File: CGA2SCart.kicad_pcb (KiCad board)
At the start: 2 copper layers, 57.1 x 62.2 mm, 25 parts, among them J1 SCART-F, J2 DB9_Male, J3 Audio-Jack-3_2Switches, Q1 2N7000

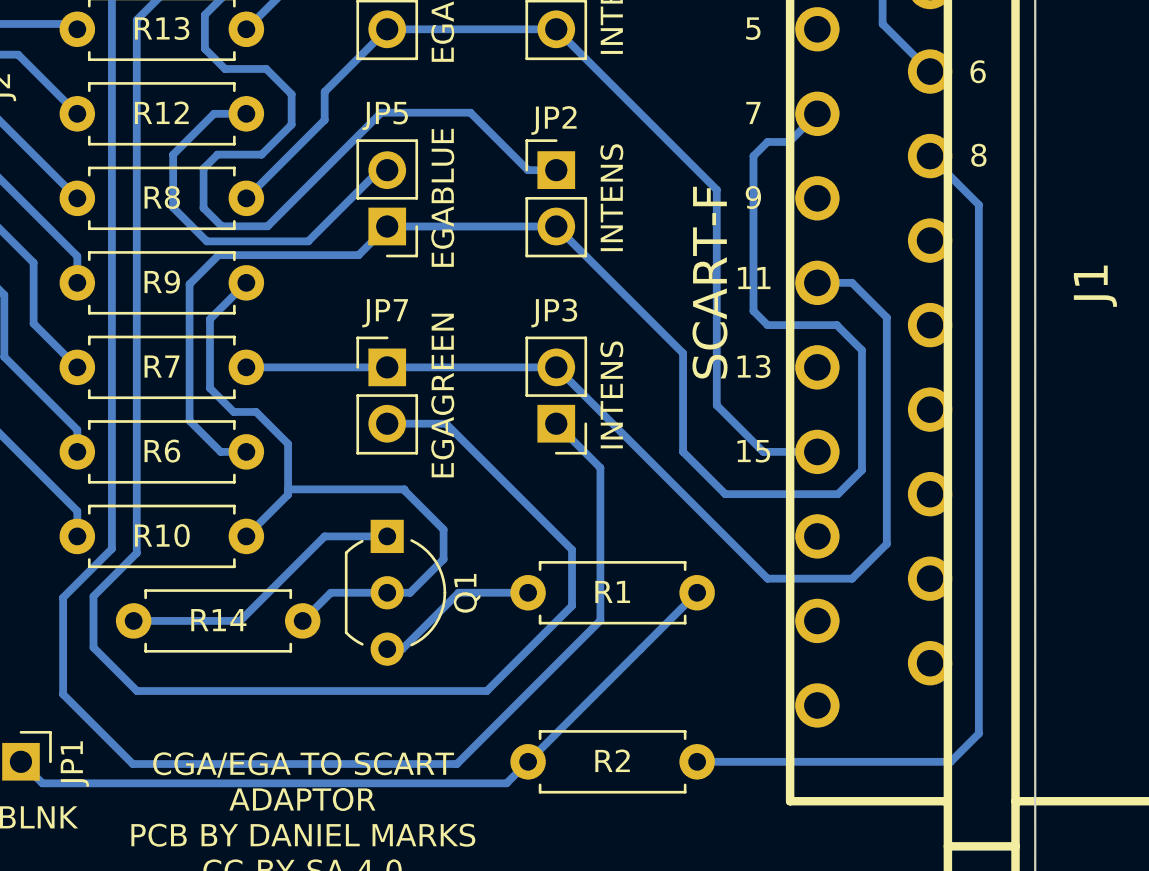
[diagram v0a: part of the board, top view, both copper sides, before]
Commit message: Corrected sync problem
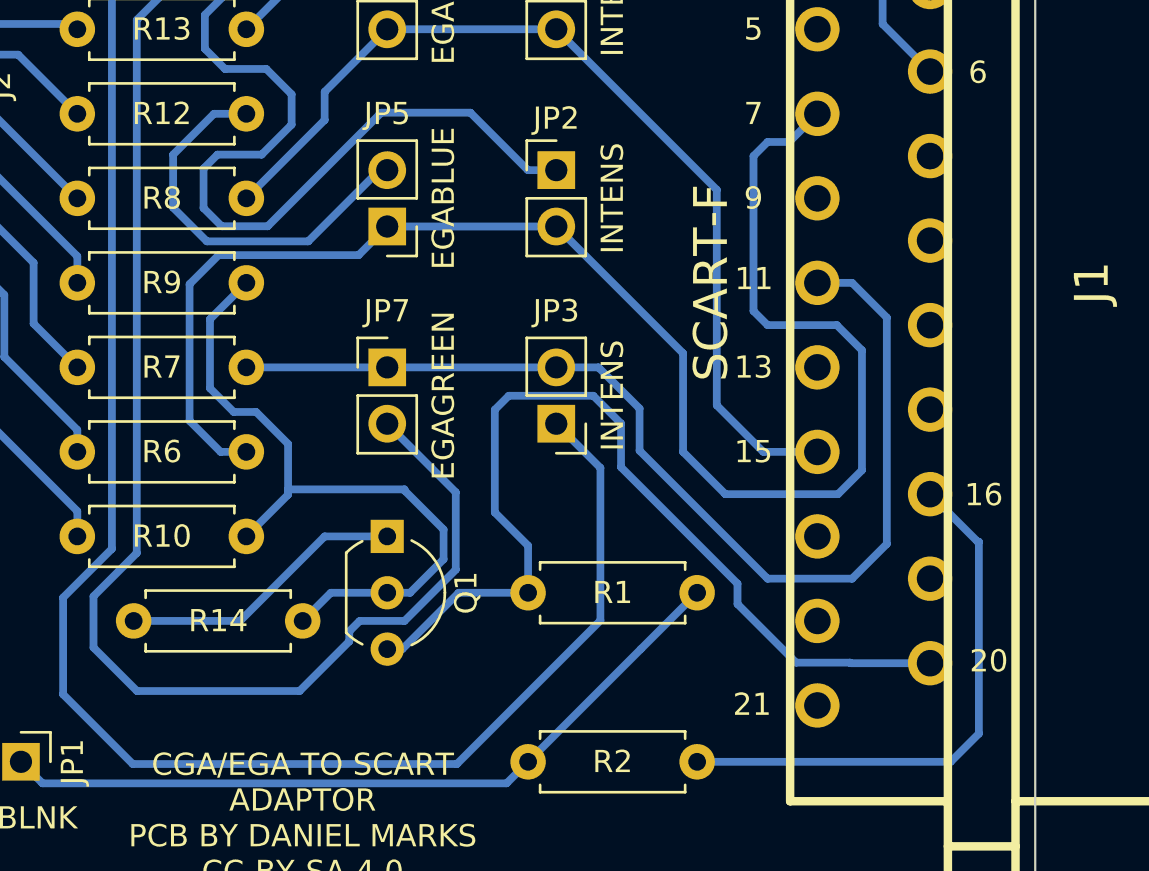
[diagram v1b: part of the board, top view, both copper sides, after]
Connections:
- J1 pad 16: unconnected-(J1-Pad16) -> Net-(J1-Pad16)
- J1 pad 20: unconnected-(J1-Pad20) -> Net-(Q1-Pad3)
- J1 pad 21: unconnected-(J1-Pad21) -> GND
- J1 pad 8: Net-(J1-Pad8) -> unconnected-(J1-Pad8)
- R2 pad 1: Net-(J1-Pad8) -> Net-(J1-Pad16)
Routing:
- net Net-(J1-Pad8): track 40.2 -> 0.00 mm
- net Net-(Q1-Pad3): track 7.40 -> 42.8 mm
- net Net-(J1-Pad16): track 0.00 -> 25.0 mm
- net Net-(JP7-Pad2): track 72.6 -> 63.0 mm
- net Net-(J1-Pad11): track 47.4 -> 48.6 mm
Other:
- board text added: "16"
- board text added: "20"
- board text added: "21"
- board text removed: "8"

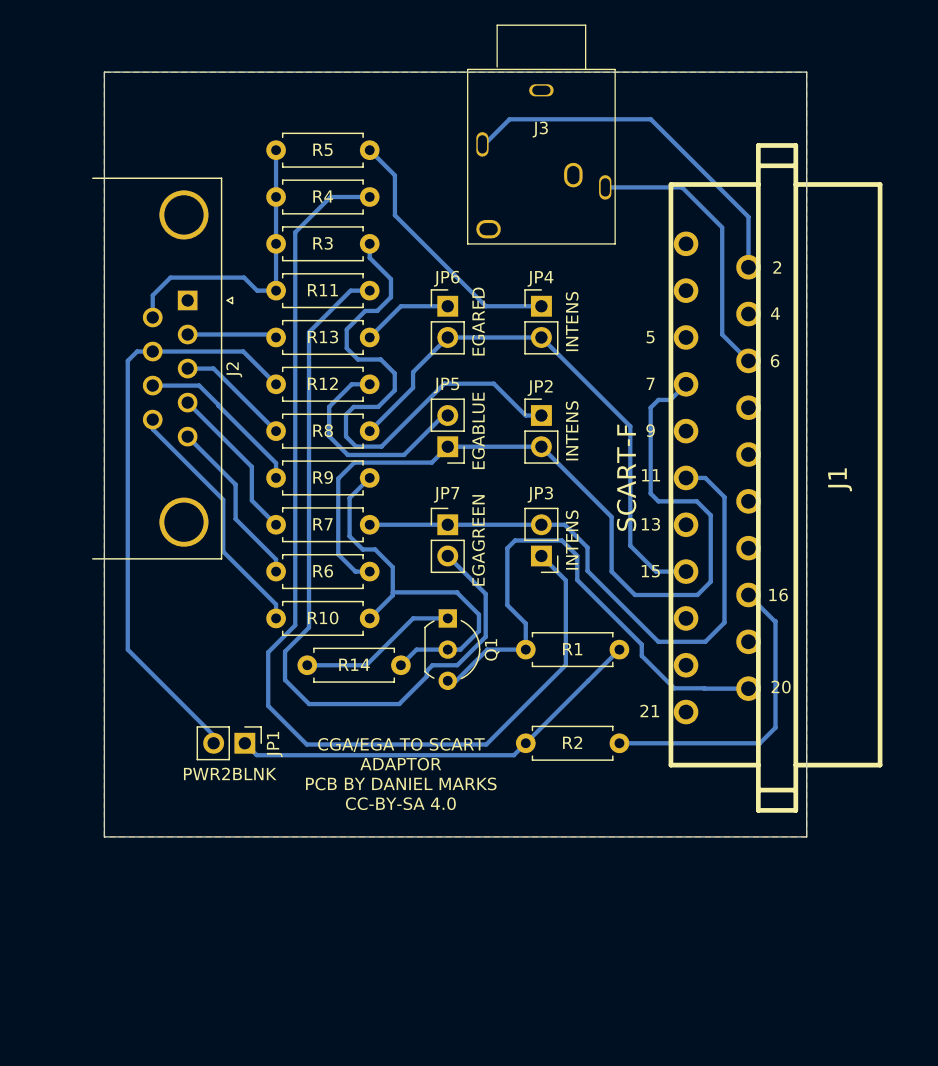
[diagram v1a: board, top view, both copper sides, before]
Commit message: Added a VGA port
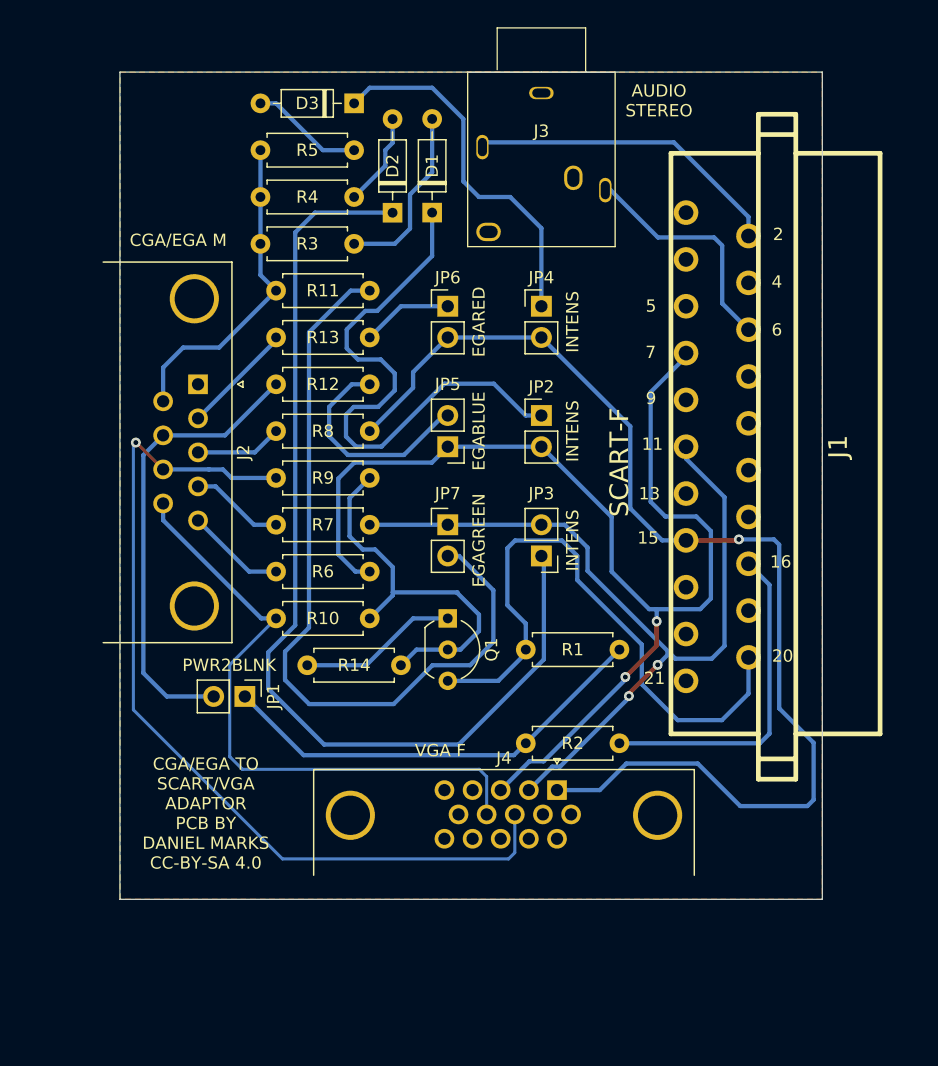
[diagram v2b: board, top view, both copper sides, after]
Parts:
- added D1: 1N4148, Diode_THT:D_DO-35_SOD27_P7.62mm_Horizontal, F.Cu at (127.0, 59.7)
- added D2: 1N4148, Diode_THT:D_DO-35_SOD27_P7.62mm_Horizontal, F.Cu at (123.8, 59.7)
- added D3: 1N4148, Diode_THT:D_DO-35_SOD27_P7.62mm_Horizontal, F.Cu at (120.7, 50.8)
- added J4: DB15_Female_HighDensity, Connector_Dsub:DSUB-15-HD_Female_Horizontal_P2.29x1.98mm_EdgePinOffset3.03mm_Housed_MountingHolesOffset4.94mm, F.Cu at (137.2, 106.7)
- R3, R4, R5: value 1k -> 330R
- moved J2 6.87 mm to (108.0, 73.7)
- moved JP1 3.81 mm to (111.8, 99.1)
- moved J1 2.54 mm to (154.9, 78.7)
- moved R3 1.27 mm to (113.0, 62.2)
- moved R4 1.27 mm to (113.0, 58.4)
- moved R5 1.27 mm to (113.0, 54.6)
- moved J3 0.22 mm to (135.9, 48.3)
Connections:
- R3 pad 2: Net-(JP2-Pad1) -> Net-(R3-Pad2)
- R4 pad 2: Net-(JP3-Pad1) -> Net-(R4-Pad2)
- R5 pad 2: Net-(JP4-Pad1) -> Net-(R5-Pad2)
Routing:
- net Net-(J2-Pad8): track 13.9 -> 73.8 mm, vias 0 -> 1
- net Net-(J1-Pad15): track 43.2 -> 93.5 mm, vias 0 -> 1
- net Net-(J2-Pad9): track 20.3 -> 51.3 mm
- net Net-(J1-Pad7): track 70.4 -> 94.5 mm, vias 0 -> 2
- net Net-(J1-Pad11): track 48.6 -> 68.8 mm, vias 0 -> 2
- net Net-(R3-Pad2): track 0.00 -> 14.7 mm
- net Net-(J2-Pad7): track 47.5 -> 37.4 mm
- net Net-(R5-Pad2): track 0.00 -> 9.20 mm
- net Net-(JP4-Pad1): track 21.1 -> 29.8 mm
- net Net-(R4-Pad2): track 0.00 -> 7.64 mm
- net Net-(J1-Pad20): track 42.8 -> 49.3 mm
- net Net-(R6-Pad1): track 14.0 -> 8.07 mm
- net Net-(J2-Pad4): track 12.9 -> 7.64 mm
- net Net-(J1-Pad2): track 29.9 -> 25.9 mm
- net Net-(J1-Pad6): track 22.6 -> 19.1 mm
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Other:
- board size 57.1 x 62.2 mm -> 57.2 x 67.3 mm
- board text added: "AUDIO STEREO"
- board text added: "CGA/EGA M"
- board text added: "CGA/EGA TO SCART/VGA ADAPTOR PCB BY DANIEL MARKS CC-BY-SA 4.0"
- board text added: "VGA F"
- board text removed: "CGA/EGA TO SCART ADAPTOR PCB BY DANIEL MARKS CC-BY-SA 4.0"

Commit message: Put SCART connector on the right way...
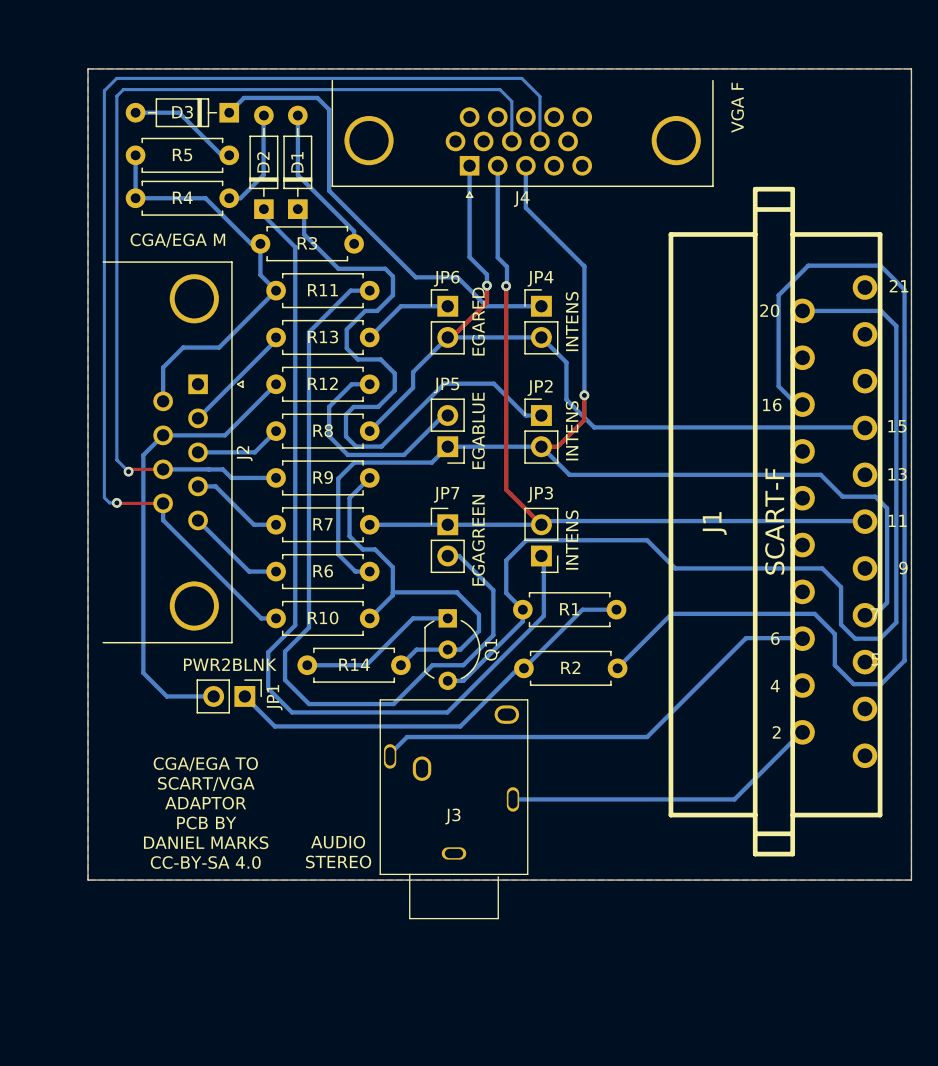
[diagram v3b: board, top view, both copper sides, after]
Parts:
- moved J3 65.7 mm to (128.8, 113.5), turned to 180 degrees
- moved J4 51.3 mm to (130.0, 55.9), turned to 180 degrees
- moved D1 10.9 mm to (116.1, 59.4)
- moved D2 10.5 mm to (113.3, 59.4)
- moved D3 10.2 mm to (110.5, 51.6)
- moved R5 10.2 mm to (102.9, 55.0)
- moved R4 10.2 mm to (102.9, 58.5)
- moved R2 6.10 mm to (142.1, 96.8)
- moved J1 6.10 mm to (154.9, 84.8), turned to -90 degrees
- moved R1 3.26 mm to (142.0, 92.0)
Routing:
- net Net-(J1-Pad16): track 27.1 -> 81.5 mm
- net Net-(J2-Pad9): track 51.3 -> 92.1 mm, vias 0 -> 1
- net Net-(J1-Pad20): track 49.3 -> 84.7 mm
- net Net-(J1-Pad15): track 93.5 -> 64.3 mm
- net Net-(J1-Pad6): track 19.1 -> 36.9 mm
- net Net-(D2-Pad1): track 82.3 -> 72.4 mm
- net Net-(J2-Pad6): track 26.5 -> 34.1 mm
- net Net-(D3-Pad1): track 29.8 -> 36.8 mm
- net Net-(J2-Pad8): track 73.8 -> 79.3 mm
- net Net-(D1-Pad1): track 46.6 -> 51.0 mm
- net Net-(D1-Pad2): track 14.7 -> 12.3 mm
- net Net-(J1-Pad11): track 68.8 -> 70.4 mm, vias 2 -> 1
- net Net-(J1-Pad7): track 94.5 -> 93.3 mm, vias 2 -> 1
- net Net-(JP1-Pad1): track 36.0 -> 35.2 mm
- net Net-(D2-Pad2): track 7.64 -> 8.43 mm
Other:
- board size 57.2 x 67.3 mm -> 67 x 66 mm

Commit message: Fixed problem with VGA pins...
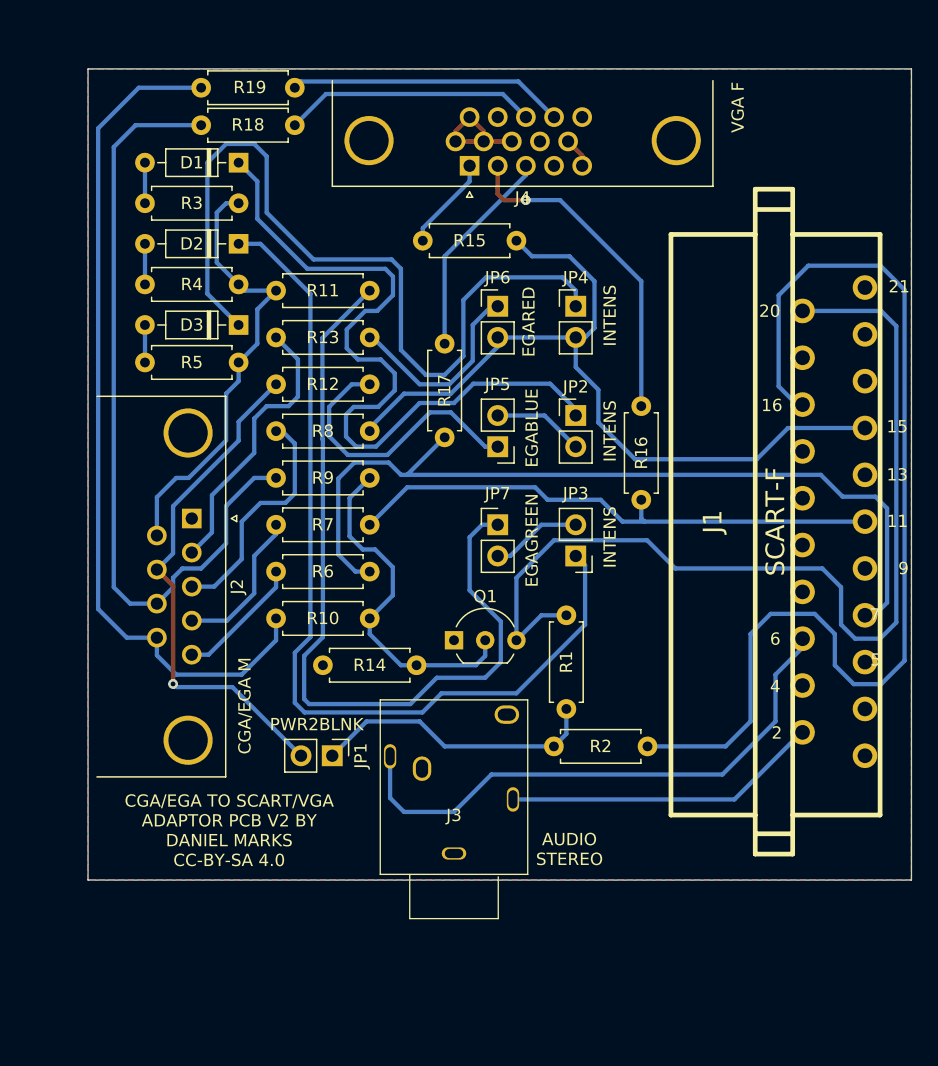
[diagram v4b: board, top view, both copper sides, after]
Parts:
- added R15: 100R, Resistor_THT:R_Axial_DIN0207_L6.3mm_D2.5mm_P7.62mm_Horizontal, F.Cu at (126.2, 62.0)
- added R16: 100R, Resistor_THT:R_Axial_DIN0207_L6.3mm_D2.5mm_P7.62mm_Horizontal, F.Cu at (144.0, 75.4)
- added R17: 100R, Resistor_THT:R_Axial_DIN0207_L6.3mm_D2.5mm_P7.62mm_Horizontal, F.Cu at (128.0, 70.4)
- added R18: 330R, Resistor_THT:R_Axial_DIN0207_L6.3mm_D2.5mm_P7.62mm_Horizontal, F.Cu at (108.2, 52.6)
- added R19: 330R, Resistor_THT:R_Axial_DIN0207_L6.3mm_D2.5mm_P7.62mm_Horizontal, F.Cu at (108.2, 49.5)
- moved R5 18.8 mm to (111.3, 71.9), turned to 180 degrees
- moved D3 17.3 mm to (111.3, 68.8)
- moved J2 10.9 mm to (107.4, 84.6)
- moved R4 10.9 mm to (111.3, 65.5), turned to 180 degrees
- moved R1 9.05 mm to (137.9, 100.1), turned to 90 degrees
- moved JP1 8.59 mm to (118.9, 103.9)
- moved R10 7.62 mm to (114.3, 92.7), turned to 0 degrees
- moved R11 7.62 mm to (114.3, 66.0), turned to 0 degrees
- moved R9 7.62 mm to (114.3, 81.3), turned to 0 degrees
- moved R2 6.80 mm to (144.5, 103.1)
- moved D1 6.13 mm to (111.3, 55.6), turned to 180 degrees
- moved JP5 4.06 mm to (132.3, 78.7)
- moved JP6 4.06 mm to (132.3, 67.3)
- moved JP7 4.06 mm to (132.3, 85.1)
- moved R3 3.75 mm to (111.3, 58.9), turned to 180 degrees
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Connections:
- net Net-(J2-Pad2) renamed EGA_RED
- net Net-(J2-Pad3) renamed CGA_RED
- net Net-(J2-Pad4) renamed CGA_GREEN
- net Net-(J2-Pad5) renamed CGA_BLUE
- net Net-(J2-Pad7) renamed EGA_BLUE
- J2 pad 6: Net-(J2-Pad6) -> INTENS_EGA_GREEN
- J2 pad 8: Net-(J2-Pad8) -> CGA_HSYNC
- J2 pad 9: Net-(J2-Pad9) -> CGA_VSYNC
- J4 pad 1: Net-(J1-Pad15) -> VGA_RED
- J4 pad 10: unconnected-(J4-Pad10) -> GND
- J4 pad 11: unconnected-(J4-Pad11) -> GND
- J4 pad 13: unconnected-(J4-Pad13) -> VGA_HSYNC
- J4 pad 14: unconnected-(J4-Pad14) -> VGA_VSYNC
- J4 pad 2: Net-(J1-Pad11) -> VGA_GREEN
- J4 pad 3: Net-(J1-Pad7) -> VGA_BLUE
- J4 pad 6: unconnected-(J4-Pad6) -> GND
- J4 pad 7: unconnected-(J4-Pad7) -> GND
- J4 pad 8: Net-(J2-Pad8) -> GND
- J4 pad 9: Net-(J2-Pad9) -> unconnected-(J4-Pad9)
- JP2 pad 2: Net-(J1-Pad7) -> Net-(JP2-Pad2)
- JP3 pad 2: Net-(J1-Pad11) -> Net-(JP3-Pad2)
- JP5 pad 1: Net-(J1-Pad7) -> Net-(JP5-Pad1)
- JP5 pad 2: Net-(JP5-Pad2) -> Net-(JP2-Pad2)
- JP7 pad 1: Net-(J1-Pad11) -> Net-(R11-Pad2)
- JP7 pad 2: Net-(JP7-Pad2) -> Net-(JP3-Pad2)
- R10 pad 1: Net-(Q1-Pad2) -> CGA_VSYNC
- R10 pad 2: Net-(J2-Pad9) -> Net-(Q1-Pad2)
- R11 pad 1: Net-(JP7-Pad2) -> INTENS_EGA_GREEN
- R11 pad 2: Net-(J2-Pad6) -> Net-(R11-Pad2)
- R12 pad 2: Net-(JP5-Pad2) -> Net-(JP5-Pad1)
- R3 pad 1: Net-(J2-Pad6) -> INTENS_EGA_GREEN
- R4 pad 1: Net-(J2-Pad6) -> INTENS_EGA_GREEN
- R5 pad 1: Net-(J2-Pad6) -> INTENS_EGA_GREEN
- R9 pad 1: Net-(Q1-Pad2) -> CGA_HSYNC
- R9 pad 2: Net-(J2-Pad8) -> Net-(Q1-Pad2)
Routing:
- net Net-(J2-Pad9): track 92.1 -> 0.00 mm, vias 1 -> 0
- net Net-(J2-Pad8): track 79.3 -> 0.00 mm, vias 1 -> 0
- net CGA_VSYNC: track 0.00 -> 69.3 mm
- net Net-(R11-Pad2): track 0.00 -> 67.0 mm
- net Net-(JP7-Pad2): track 64.0 -> 0.00 mm
- net CGA_HSYNC: track 0.00 -> 63.9 mm
- net INTENS_EGA_GREEN: track 0.00 -> 36.5 mm
- net Net-(J2-Pad6): track 34.1 -> 0.00 mm
- net Net-(D3-Pad1): track 36.8 -> 66.9 mm
- net VGA_GREEN: track 0.00 -> 27.1 mm, vias 0 -> 1
- net Net-(J1-Pad11): track 70.4 -> 44.6 mm, vias 1 -> 0
- net Net-(J1-Pad7): track 93.3 -> 69.5 mm, vias 1 -> 0
- net Net-(JP5-Pad1): track 0.00 -> 23.4 mm
- net VGA_VSYNC: track 0.00 -> 22.5 mm
- net VGA_HSYNC: track 0.00 -> 20.6 mm
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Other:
- board text added: "CGA/EGA TO SCART/VGA ADAPTOR PCB V2 BY DANIEL MARKS CC-BY-SA 4.0"
- board text removed: "CGA/EGA TO SCART/VGA ADAPTOR PCB BY DANIEL MARKS CC-BY-SA 4.0"

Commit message: Other connections fixed
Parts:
- moved JP5 2.55 mm to (132.3, 76.2), turned to 0 degrees
- moved JP7 2.54 mm to (132.3, 87.6), turned to 180 degrees
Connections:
- JP2 pad 2: Net-(JP2-Pad2) -> Net-(J1-Pad7)
- JP3 pad 2: Net-(JP3-Pad2) -> Net-(J1-Pad11)
- JP5 pad 2: Net-(JP2-Pad2) -> Net-(J1-Pad7)
- JP7 pad 2: Net-(JP3-Pad2) -> Net-(J1-Pad11)
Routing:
- net Net-(J1-Pad7): track 69.5 -> 80.5 mm
- net Net-(JP3-Pad2): track 7.40 -> 0.00 mm
- net Net-(JP2-Pad2): track 7.40 -> 0.00 mm
- net Net-(J1-Pad11): track 44.6 -> 49.9 mm
- net Net-(JP7-Pad1): track 67.0 -> 61.8 mm
- net Net-(JP5-Pad1): track 23.4 -> 22.3 mm
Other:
- board text added: "CGA/EGA TO SCART/VGA PCB V2 BY DANIEL MARKS CC-BY-SA 4.0(VGA MONITOR MUST SUPPORT 15 KHZ SCAN)"
- board text removed: "CGA/EGA TO SCART/VGA ADAPTOR PCB V2 BY DANIEL MARKS CC-BY-SA 4.0"
